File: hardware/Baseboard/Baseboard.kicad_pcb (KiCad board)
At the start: 2 copper layers, 160 x 160 mm, 71 parts, among them IC1 74HC00, IC10 W65C22, IC2 W65C02, IC3 74HC138, IC4 SYSTEM ROM, IC5 RAM, IC6 W65C22, IC7 W65C51, IC8 TL7702A, IC9 FT232RL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

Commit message: Add switch to select between oscillator as clock and manual clock source
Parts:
- added C19: 100nF, Capacitor_THT:C_Rect_L4.0mm_W2.5mm_P2.50mm, F.Cu at (229.8, 155.4)
- added R10: 10k, Resistor_THT:R_Axial_DIN0207_L6.3mm_D2.5mm_P7.62mm_Horizontal, F.Cu at (148.0, 166.9)
- added R2: 10k, Resistor_THT:R_Axial_DIN0207_L6.3mm_D2.5mm_P7.62mm_Horizontal, F.Cu at (166.0, 78.0)
- added SW6: CLOCK, Button_Switch_THT:SW_PUSH_6mm_H4.3mm, F.Cu at (147.2, 163.5)
- added SW7: CLOCK INPUT, Button_Switch_THT:SW_E-Switch_EG1271_DPDT, F.Cu at (220.9, 155.4)
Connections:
- net /IO/~RESET renamed /IO/~Reset
- XTAL1 pad 8: /IO/Clock -> /Processor/OSC
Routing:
- net /Processor/CLOCK_SWITCH: track 0.00 -> 99.8 mm
- net /Processor/OSC: track 0.00 -> 21.4 mm
- net /IO/Clock: track 235.7 -> 245.6 mm, vias 10 -> 11
- net /IO/A0: track 416.1 -> 412.0 mm
- net /IO/A1: track 418.8 -> 414.7 mm
- net /IO/A2: track 363.9 -> 359.8 mm
- net /IO/A3: track 366.2 -> 362.0 mm
- net /IO/R~W: vias 12 -> 10
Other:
- board text added: "BTN"
- board text added: "OSC"

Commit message: Add switch for clock selection
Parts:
- SW7: footprint Button_Switch_THT:SW_E-Switch_EG1271_DPDT -> Switches:SW_E-Switch_EG1271_DPDT
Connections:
- net /Processor/CLOCK_SWITCH renamed /Processor/CLOCK_BTN
- net /Processor/OSC renamed /Processor/CLOCK_OSC
- IC10 pad 13: Net-(IC10-Pad13) -> (no net)
- IC10 pad 14: Net-(IC10-Pad14) -> (no net)
- IC10 pad 15: Net-(IC10-Pad15) -> (no net)
- IC10 pad 18: Net-(IC10-Pad18) -> (no net)
- IC10 pad 19: Net-(IC10-Pad19) -> (no net)
- IC10 pad 39: Net-(IC10-Pad39) -> (no net)
- IC10 pad 40: Net-(IC10-Pad40) -> (no net)
- IC2 pad 1: Net-(IC2-Pad1) -> (no net)
- IC2 pad 3: Net-(IC2-Pad3) -> (no net)
- IC2 pad 35: Net-(IC2-Pad35) -> (no net)
- IC2 pad 36: Net-(IC2-Pad36) -> (no net)
- IC2 pad 38: Net-(IC2-Pad38) -> (no net)
- IC2 pad 39: Net-(IC2-Pad39) -> (no net)
- IC2 pad 5: Net-(IC2-Pad5) -> (no net)
- IC2 pad 7: Net-(IC2-Pad7) -> (no net)
- IC3 pad 10: Net-(IC3-Pad10) -> (no net)
- IC3 pad 11: Net-(IC3-Pad11) -> (no net)
- IC3 pad 12: Net-(IC3-Pad12) -> (no net)
- IC3 pad 7: Net-(IC3-Pad7) -> (no net)
- IC3 pad 9: Net-(IC3-Pad9) -> (no net)
- IC6 pad 39: Net-(IC6-Pad39) -> (no net)
- IC6 pad 40: Net-(IC6-Pad40) -> (no net)
- IC7 pad 5: Net-(IC7-Pad5) -> (no net)
- IC8 pad 6: Net-(IC8-Pad6) -> (no net)
- IC9 pad 10: Net-(IC9-Pad10) -> (no net)
- IC9 pad 12: Net-(IC9-Pad12) -> (no net)
- IC9 pad 13: Net-(IC9-Pad13) -> (no net)
- IC9 pad 14: Net-(IC9-Pad14) -> (no net)
- IC9 pad 26: Net-(IC9-Pad26) -> (no net)
- IC9 pad 27: Net-(IC9-Pad27) -> (no net)
- IC9 pad 28: Net-(IC9-Pad28) -> (no net)
- IC9 pad 6: Net-(IC9-Pad6) -> (no net)
- IC9 pad 9: Net-(IC9-Pad9) -> (no net)
- RV1 pad 3: Net-(RV1-Pad3) -> (no net)
- X2 pad 1: Net-(X2-Pad1) -> (no net)
- X3 pad 28: Net-(X3-Pad28) -> (no net)
- X3 pad 30: Net-(X3-Pad30) -> (no net)
- X3 pad 32: Net-(X3-Pad32) -> (no net)
- X3 pad 33: Net-(X3-Pad33) -> (no net)
- X3 pad 34: Net-(X3-Pad34) -> (no net)
- X3 pad 35: Net-(X3-Pad35) -> (no net)
- X3 pad 36: Net-(X3-Pad36) -> (no net)
- X3 pad 37: Net-(X3-Pad37) -> (no net)
- X3 pad 38: Net-(X3-Pad38) -> (no net)
- X4 pad 3: Net-(X4-Pad3) -> (no net)
- X4 pad 6: Net-(X4-Pad6) -> (no net)
- XTAL1 pad 1: Net-(XTAL1-Pad1) -> (no net)

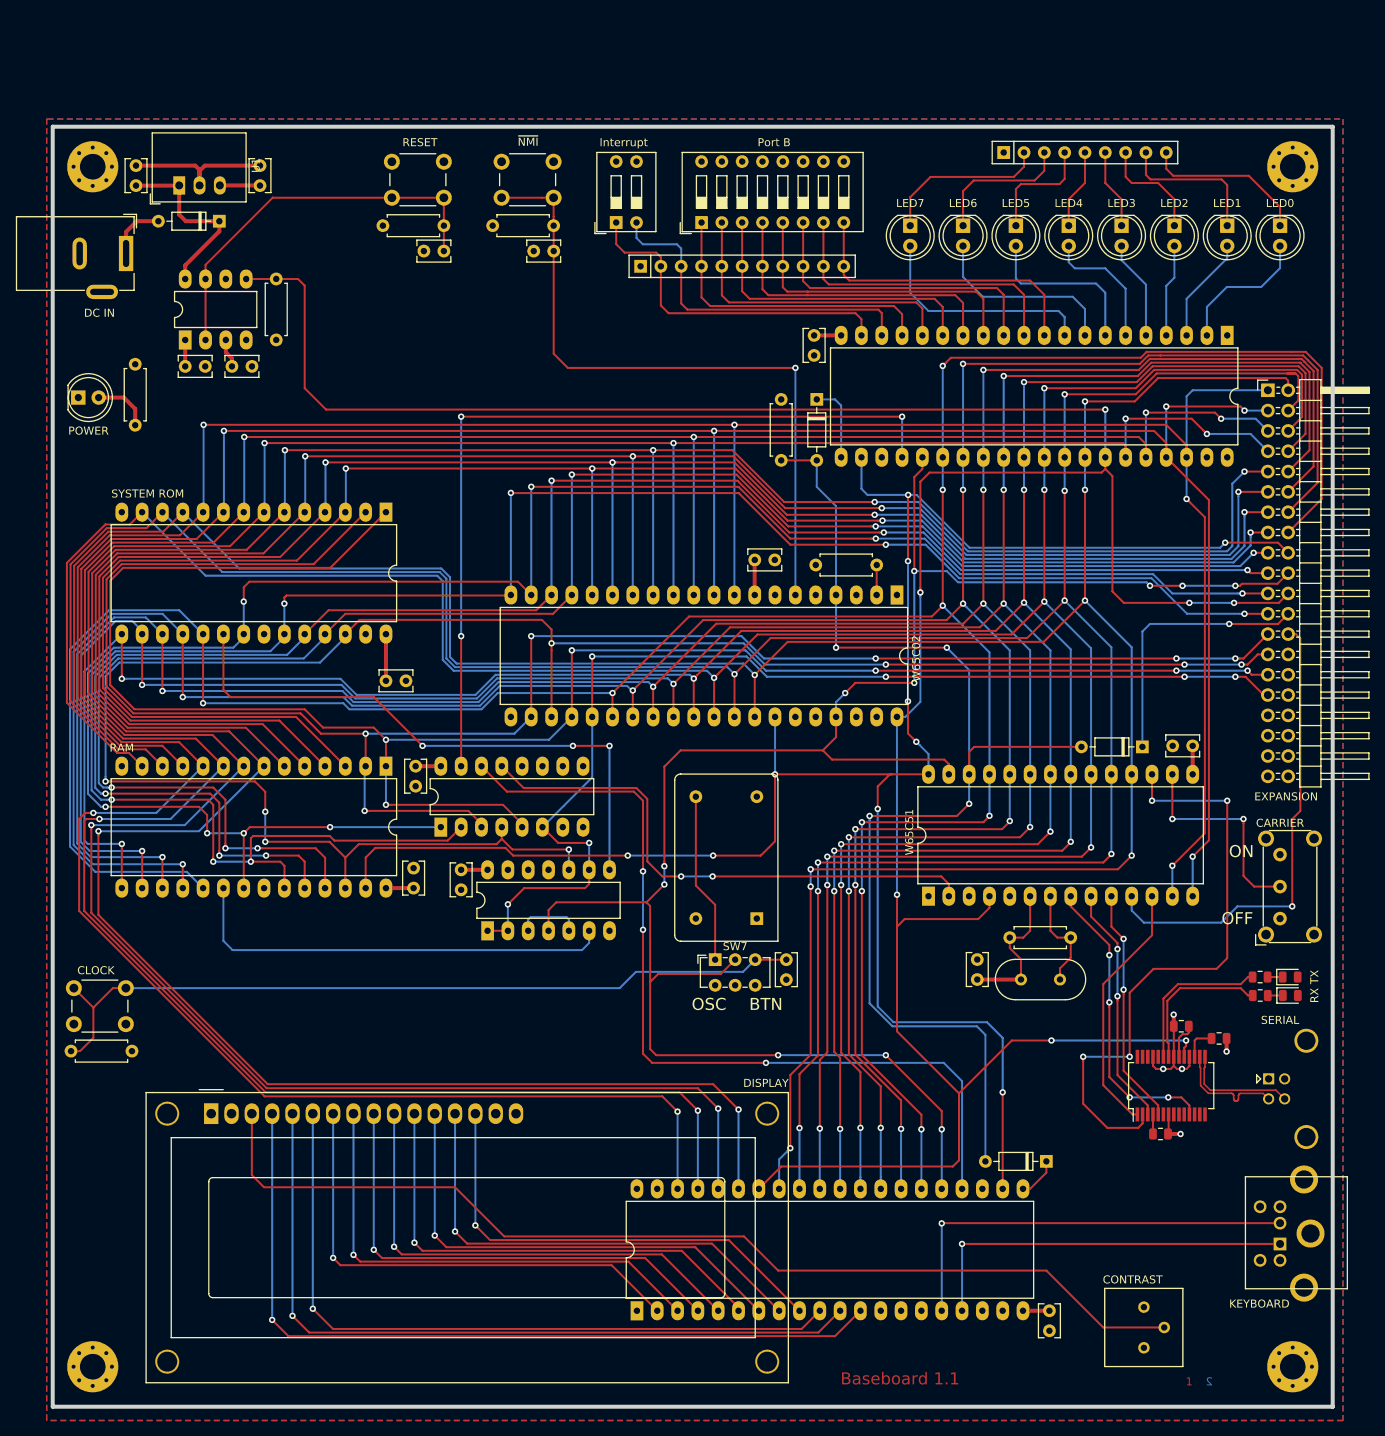
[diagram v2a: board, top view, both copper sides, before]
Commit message: Rework hardware for IRQ, change some routing
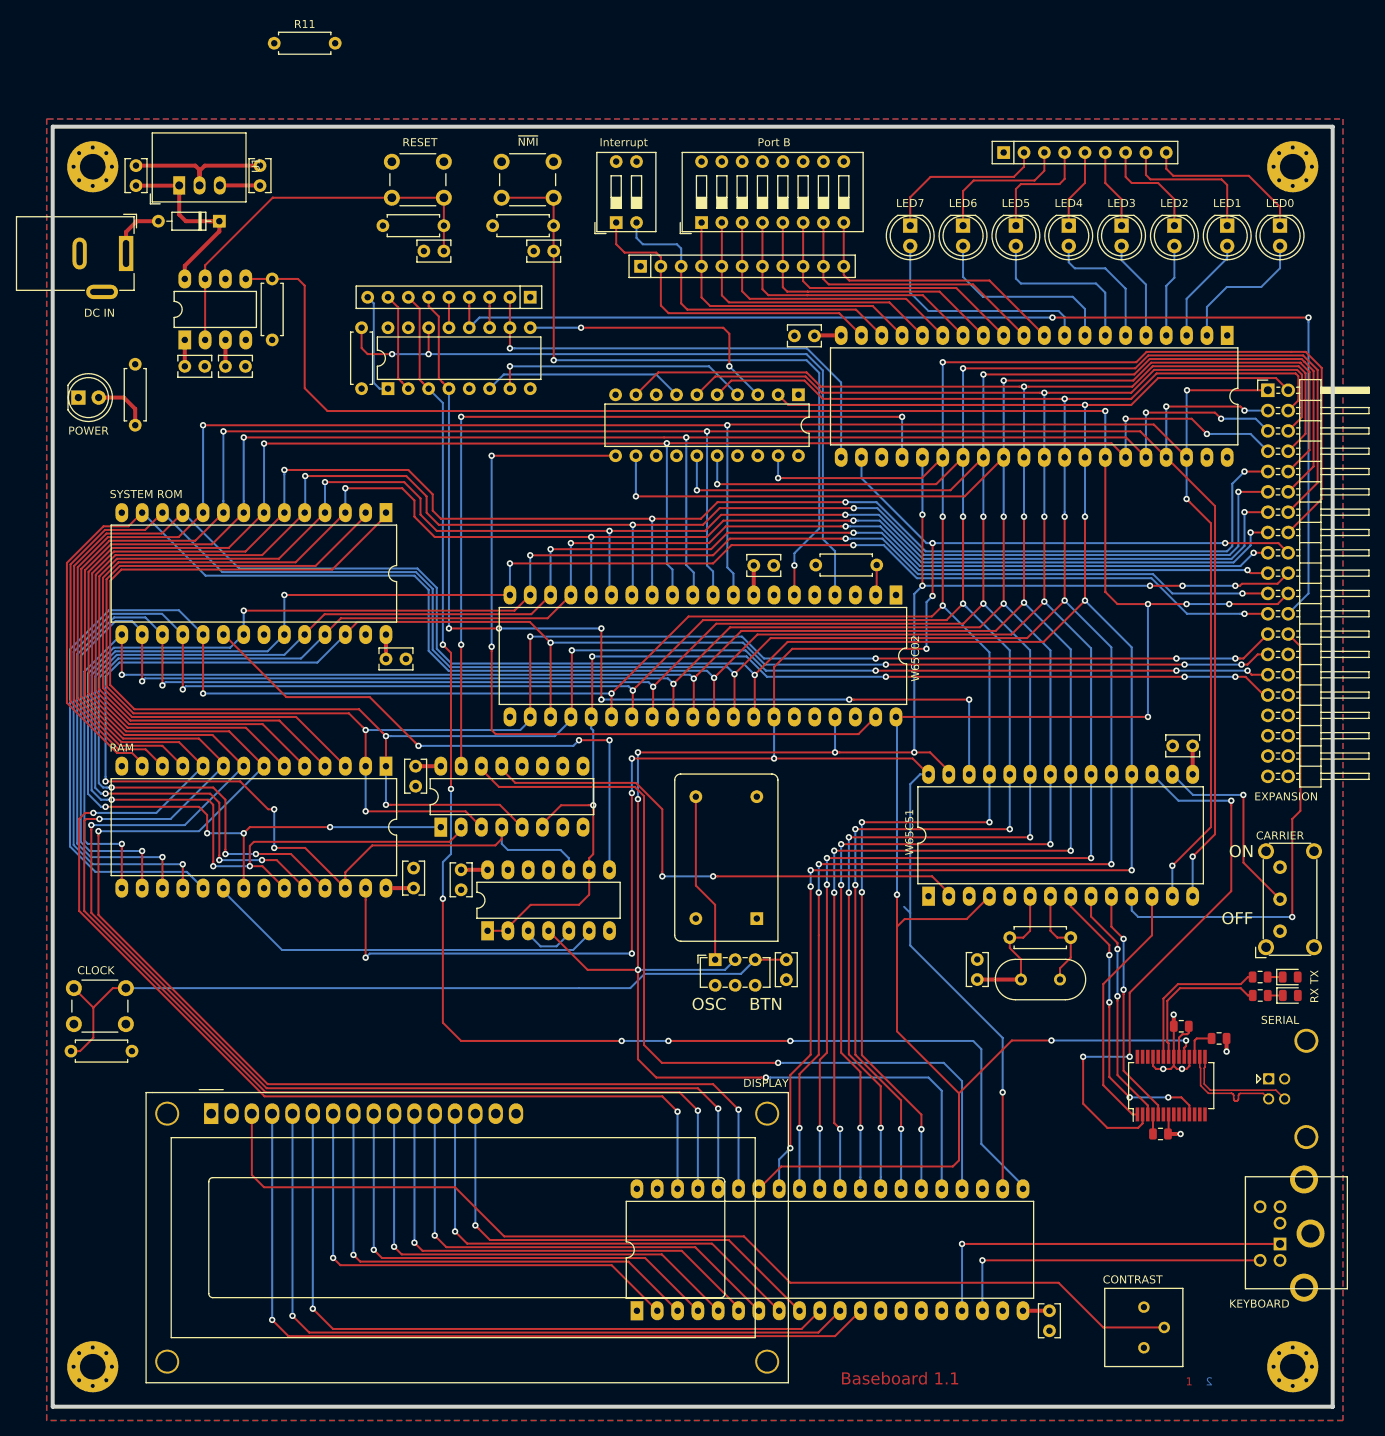
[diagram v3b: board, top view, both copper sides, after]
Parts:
- removed D14, D8, D9: SD103A, Diode_THT:D_DO-35_SOD27_P7.62mm_Horizontal
- added IC11: 74HC148, Package_DIP:DIP-16_W7.62mm, F.Cu at (180.0, 84.1)
- added IC12: 74HC273, Package_DIP:DIP-20_W7.62mm, F.Cu at (231.3, 84.8)
- added R11: 10k, Resistor_THT:R_Axial_DIN0207_L6.3mm_D2.5mm_P7.62mm_Horizontal, F.Cu at (165.7, 40.9)
- added RN3: 4k7, Resistor_THT:R_Array_SIP9, F.Cu at (197.7, 72.6)
- C8: value 100nF -> 30pF
- moved R1 53.2 mm to (176.7, 84.1)
- moved C4 2.74 mm to (179.7, 117.8)
- moved SW5 1.58 mm to (291.5, 151.9)
- moved C12 0.81 mm to (159.6, 81.3)
- moved C2 0.70 mm to (225.7, 106.2)
- moved R2 0.51 mm to (165.5, 78.0)
- moved IC2 0.12 mm to (243.5, 109.8)
- moved C7 0.07 mm to (233.3, 77.5), turned to 180 degrees
- moved IC4 0.06 mm to (179.7, 99.5)
- moved IC8 0.05 mm to (154.6, 78.0)
- moved C13 0.05 mm to (154.6, 81.3)
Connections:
- IC10 pad 13: (no net) -> Net-(IC10-Pad13)
- IC10 pad 14: (no net) -> Net-(IC10-Pad14)
- IC10 pad 15: (no net) -> Net-(IC10-Pad15)
- IC10 pad 16: /LCD / PS2/PS20 -> Net-(IC10-Pad16)
- IC10 pad 18: (no net) -> /LCD / PS2/PS20
- IC10 pad 19: (no net) -> Net-(IC10-Pad19)
- IC10 pad 21: /Processor/~IRQ_VIA_2 -> /IRQ/~IRQ_VIA_2
- IC10 pad 39: (no net) -> Net-(IC10-Pad39)
- IC10 pad 40: (no net) -> Net-(IC10-Pad40)
- IC2 pad 1: (no net) -> Net-(IC2-Pad1)
- IC2 pad 3: (no net) -> Net-(IC2-Pad3)
- IC2 pad 35: (no net) -> Net-(IC2-Pad35)
- IC2 pad 36: (no net) -> Net-(IC2-Pad36)
- IC2 pad 38: (no net) -> Net-(IC2-Pad38)
- IC2 pad 39: (no net) -> /IRQ/IRQ_Sync
- IC2 pad 4: /Processor/~IRQ_ACIA -> /IRQ/~IRQ_CPU
- IC2 pad 5: (no net) -> Net-(IC2-Pad5)
- IC2 pad 7: (no net) -> Net-(IC2-Pad7)
- IC3 pad 10: (no net) -> Net-(IC3-Pad10)
- IC3 pad 11: (no net) -> Net-(IC3-Pad11)
- IC3 pad 12: (no net) -> Net-(IC3-Pad12)
- IC3 pad 7: (no net) -> Net-(IC3-Pad7)
- IC3 pad 9: (no net) -> Net-(IC3-Pad9)
- IC6 pad 21: /Processor/~IRQ_VIA_1 -> /IRQ/~IRQ_VIA_1
- IC6 pad 39: (no net) -> Net-(IC6-Pad39)
- IC6 pad 40: (no net) -> Net-(IC6-Pad40)
- IC7 pad 26: /Processor/~IRQ_ACIA -> /IRQ/~IRQ_ACIA
- IC7 pad 5: (no net) -> Net-(IC7-Pad5)
- IC8 pad 6: (no net) -> Net-(IC8-Pad6)
- IC9 pad 10: (no net) -> Net-(IC9-Pad10)
- IC9 pad 12: (no net) -> Net-(IC9-Pad12)
- IC9 pad 13: (no net) -> Net-(IC9-Pad13)
- IC9 pad 14: (no net) -> Net-(IC9-Pad14)
- IC9 pad 26: (no net) -> Net-(IC9-Pad26)
- IC9 pad 27: (no net) -> Net-(IC9-Pad27)
- IC9 pad 28: (no net) -> Net-(IC9-Pad28)
- IC9 pad 6: (no net) -> Net-(IC9-Pad6)
- IC9 pad 9: (no net) -> Net-(IC9-Pad9)
- R1 pad 1: /Processor/~IRQ_ACIA -> +5V
- R1 pad 2: +5V -> /IRQ/~IRQ_CPU
- RV1 pad 3: (no net) -> Net-(RV1-Pad3)
- X2 pad 1: (no net) -> Net-(X2-Pad1)
- X3 pad 28: (no net) -> Net-(X3-Pad28)
- X3 pad 30: (no net) -> Net-(X3-Pad30)
- X3 pad 32: (no net) -> Net-(X3-Pad32)
- X3 pad 33: (no net) -> Net-(X3-Pad33)
- X3 pad 34: (no net) -> Net-(X3-Pad34)
- X3 pad 35: (no net) -> Net-(X3-Pad35)
- X3 pad 36: (no net) -> Net-(X3-Pad36)
- X3 pad 37: (no net) -> Net-(X3-Pad37)
- X3 pad 38: (no net) -> Net-(X3-Pad38)
- X4 pad 2: /LCD / PS2/PS20 -> Net-(X4-Pad2)
- X4 pad 3: (no net) -> GND
- X4 pad 4: GND -> +5V
- X4 pad 5: +5V -> /LCD / PS2/PS20
- X4 pad 6: (no net) -> Net-(X4-Pad6)
- XTAL1 pad 1: (no net) -> Net-(XTAL1-Pad1)
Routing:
- net /IRQ/~IRQ_VIA_2: track 0.00 -> 181.6 mm, vias 0 -> 6
- net /Processor/~IRQ_ACIA: track 148.9 -> 0.00 mm, vias 4 -> 0
- net /IRQ/~IRQ_ACIA: track 0.00 -> 125.7 mm, vias 0 -> 6
- net /IO/~IRQ: track 33.6 -> 147.3 mm, vias 1 -> 2
- net /IRQ/IRQ_Sync: track 0.00 -> 98.9 mm, vias 0 -> 2
- net /IRQ/~IRQ_CPU: track 0.00 -> 93.4 mm, vias 0 -> 2
- net /IRQ/~IRQ_VIA_1: track 0.00 -> 58.9 mm, vias 0 -> 1
- net /IO/D4: track 354.4 -> 406.0 mm, vias 10 -> 11
- net /IO/D3: track 347.4 -> 395.7 mm
- net /IO/D2: track 355.4 -> 399.5 mm
- net /IO/D1: track 357.6 -> 400.4 mm
- net /IO/D5: track 359.6 -> 399.7 mm, vias 10 -> 11
- net /IO/D0: track 355.8 -> 393.3 mm
- net Net-(IC11-Pad9): track 0.00 -> 34.3 mm, vias 0 -> 2
- net /IO/D6: track 365.3 -> 398.9 mm, vias 10 -> 11
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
